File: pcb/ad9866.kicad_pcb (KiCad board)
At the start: 4 copper layers, 48.8 x 51 mm, 71 parts, among them CN1 MEC6-140_CONNECTOR_BEMICRO, CN2 PCIE, P1 CONN_4, P10 CONN_1, P13 CONN_1, P14 CONN_1, P15 Si510 73.728, P16 CONN_3X2, P17 CONN_4, P18 CONN_1, P19 CONN_1, P2 CONN_1, P20 CONN_1, P22 CONN_1, P23 CONN_5, P24 CONN_5, P25 CONN_5, P3 CONN_1, P4 CONN_1, P5 CONN_1, P6 CONN_1, P8 CONN_1, P9 CONN_1, T1 TRANSF_ADT8, T2 TRANSF_ADT2, T3 TRANSF_ADT2, U1 AD9866BCPZ, U2 NCP1117ST33T3G, U3 NCP1117ST33T3G

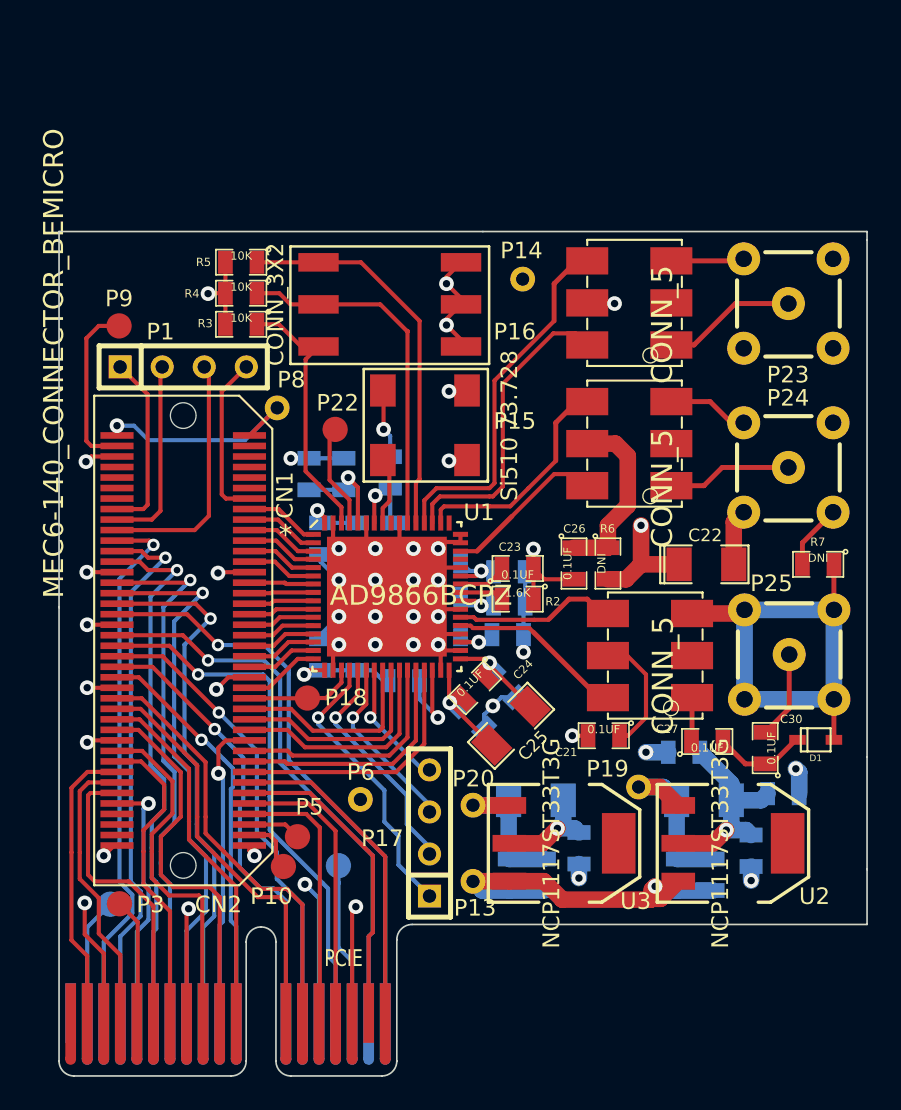
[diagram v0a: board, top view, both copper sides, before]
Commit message: adding libraries needed
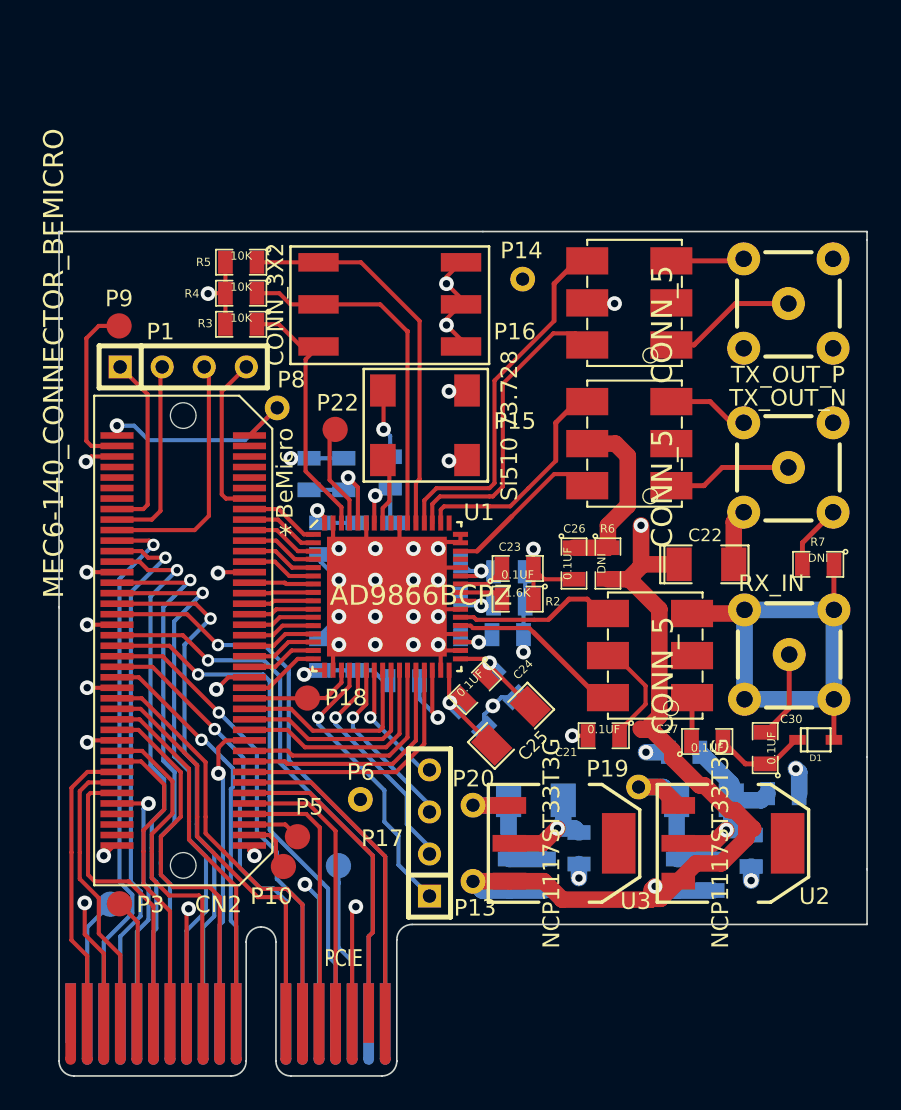
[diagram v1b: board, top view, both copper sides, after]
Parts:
- removed P23, P24, P25: CONN_5, BEMICRO:SMA
- added RX_IN: CONN_5, BEMICRO:SMA, F.Cu at (144.8, 109.0)
- added TX_OUT_N: CONN_5, BEMICRO:SMA, F.Cu at (144.8, 97.7)
- added TX_OUT_P: CONN_5, BEMICRO:SMA, F.Cu at (144.8, 87.8)
- renumbered CN1 to BeMicro
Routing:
- net VIN: track 29.4 -> 55.4 mm
- net Net-(C21-Pad1): track 7.43 -> 6.69 mm
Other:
- net class Default: trace_width 0.25 -> 0.205
- rule trace_min: 0.2 -> 0.205
